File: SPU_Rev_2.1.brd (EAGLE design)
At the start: 141 x 101.6 mm, 236 parts, among them Q1 12MHz, X1 403-5X020-5X

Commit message: renamed to 2.1
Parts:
- added C60, C61, C62, C63, C64, C65, C66, C67: 10u, rcl:E/7260-38W
- added D13: (no value), special:7SEG-13
- added RN_SEG1, RN_SEG2: 220, resistor-dil:0603-ARC
- moved C57 51.4 mm to (14.5, 21.0), turned to 270 degrees
- moved C53 49.4 mm to (29.1, 18.5), flipped to the bottom
- moved C51 49.3 mm to (29.3, 19.3), turned to 90 degrees
- moved C59 49.0 mm to (14.9, 19.4), flipped to the bottom, turned to 90 degrees
- moved C58 48.2 mm to (14.5, 18.4), turned to 180 degrees
- moved X_RXSM-DAPI 47.2 mm to (135.9, 65.8)
- moved C47 46.6 mm to (36.4, 21.8), turned to 90 degrees
- moved C54 46.2 mm to (22.6, 21.7), turned to 90 degrees
- moved R57 46.1 mm to (20.2, 19.1), turned to 180 degrees
- moved C45 46.0 mm to (39.1, 19.2), turned to 270 degrees
- moved C50 46.0 mm to (27.2, 16.3), turned to 90 degrees
- moved C46 45.2 mm to (40.1, 15.9), turned to 270 degrees
- moved R50 44.4 mm to (35.4, 19.3), turned to 180 degrees
- moved R17 43.3 mm to (121.0, 59.9), turned to 270 degrees
- moved R63 42.8 mm to (15.0, 22.9), flipped to the bottom
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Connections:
- new net N$126: D13.7, RN_SEG1.8
- new net N$140: D13.6, RN_SEG1.7
- new net N$142: D13.4, RN_SEG1.6
- new net N$143: D13.2, RN_SEG1.5
- new net N$144: D13.1, RN_SEG2.8
- new net N$145: D13.9, RN_SEG2.7
- new net N$146: D13.10, RN_SEG2.6
- new net N$147: D13.5, RN_SEG2.5
- new net N$149: RN_SEG2.1
- new net N$150: RN_SEG1.4
- new net N$151: RN_SEG1.3
- new net N$152: RN_SEG1.2
- new net N$153: RN_SEG1.1
- new net N$154: RN_SEG2.2
- new net N$155: RN_SEG2.3
- new net N$156: RN_SEG2.4
- net 28V: now also C60.+, C61.+, C62.+
- net 28VGND: now also C60.-, C61.-, C62.-
- net 3V3: now also C67.+, D13.3, D13.8
- net 5V: now also C63.+, C64.+, C65.+, C66.+
- net GND: now also C63.-, C64.-, C65.-, C66.-, C67.-
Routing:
- net DMS63: track 0.00 -> 14.0 mm
- net DMS41: track 0.00 -> 12.9 mm
- net DMS62: track 0.00 -> 12.6 mm
- net DMS42: track 0.00 -> 11.6 mm
- net DMS61: track 0.00 -> 11.5 mm
- net DMS43: track 0.00 -> 10.1 mm
- net DMS51: track 0.00 -> 3.85 mm
- net DMS53: track 0.00 -> 3.64 mm
- net DMS52: track 0.00 -> 3.32 mm

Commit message: foo
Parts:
- removed D13: (no value), special:7SEG-13
- removed RN_SEG1, RN_SEG2: 220, resistor-dil:0603-ARC
- added C68, C69, C70, C71: 10u, rcl:E/7260-38W
- added X_GPIO: 403-5X020-5X, con-ept-One27:403-5X020-5X
- moved X_MIRROR 69.1 mm to (120.5, 83.6)
- moved X_MIRROR1 69.1 mm to (120.5, 83.6)
- moved C2 47.0 mm to (84.3, 86.9), turned to 270 degrees
- moved Q1 45.4 mm to (90.7, 91.9), turned to 180 degrees
- moved D2 40.3 mm to (97.0, 91.9), turned to 0 degrees
- moved U_OPTO_2 35.6 mm to (108.2, 90.8), turned to 0 degrees
- moved U_CH340G 35.5 mm to (90.7, 81.8), turned to 180 degrees
- moved C1 34.2 mm to (97.0, 86.9), turned to 270 degrees
- moved D1 32.8 mm to (97.0, 85.6), turned to 0 degrees
- moved RN12 30.0 mm to (108.1, 87.1), turned to 90 degrees
- moved C42 29.6 mm to (96.7, 56.2), turned to 180 degrees
- moved C33 27.9 mm to (97.0, 81.0), turned to 90 degrees
- moved C62 27.7 mm to (111.6, 69.2), turned to 90 degrees
- moved U_OPTO_1 25.2 mm to (108.2, 83.8), turned to 0 degrees
- moved RN11 23.6 mm to (101.9, 79.4), turned to 0 degrees
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- renumbered X1 to X_DMS
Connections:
- removed net N$126: D13.7, RN_SEG1.8
- removed net N$140: D13.6, RN_SEG1.7
- removed net N$142: D13.4, RN_SEG1.6
- removed net N$143: D13.2, RN_SEG1.5
- removed net N$144: D13.1, RN_SEG2.8
- removed net N$145: D13.9, RN_SEG2.7
- removed net N$146: D13.10, RN_SEG2.6
- removed net N$147: D13.5, RN_SEG2.5
- removed net N$149: RN_SEG2.1
- removed net N$150: RN_SEG1.4
- removed net N$151: RN_SEG1.3
- removed net N$152: RN_SEG1.2
- removed net N$153: RN_SEG1.1
- removed net N$154: RN_SEG2.2
- removed net N$155: RN_SEG2.3
- removed net N$156: RN_SEG2.4
- net 3V3: now also C68.+, C69.+, C70.+, C71.+, X_GPIO.P$B1, X_GPIO.P$B2; no longer D13.3, D13.8
- net GND: now also C68.-, C69.-, C70.-, C71.-, X_GPIO.P$A1, X_GPIO.P$A2
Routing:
- net 28V: track 9.34 -> 97.4 mm, vias 1 -> 8
- net 5V: track 0.00 -> 37.2 mm, vias 0 -> 6
- net GND: track 37.8 -> 51.7 mm, vias 1 -> 186
- net 3V3: track 21.2 -> 32.3 mm, vias 2 -> 8
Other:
- board size 141 x 101.6 mm -> 127.6 x 101.6 mm

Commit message: viafence STRUCT
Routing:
- net GND: vias 186 -> 56
- added copper zone on layer 1, net STRUCT
- added copper zone on layer 15, net STRUCT
- added copper zone on layer 16, net STRUCT
- added copper zone on layer 2, net STRUCT

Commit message: foo
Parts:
- added C72, C73: 10u, rcl:E/7260-38W
- moved D10 35.4 mm to (99.6, 69.1), turned to 270 degrees
- moved D3 27.0 mm to (90.4, 71.6), turned to 0 degrees
- moved D4 25.9 mm to (90.4, 67.9), turned to 0 degrees
- moved RN11 18.1 mm to (114.6, 92.3), flipped to the bottom, turned to 270 degrees
- moved C36 13.5 mm to (96.3, 11.7), turned to 90 degrees
- moved R48 4.70 mm to (47.0, 22.1), turned to 180 degrees
- moved R49 3.68 mm to (42.8, 22.1), turned to 0 degrees
- moved C69 3.41 mm to (84.2, 85.0), turned to 270 degrees
- moved RN_B_PT3 1.45 mm to (18.3, 93.6)
- moved C62 1.13 mm to (111.8, 68.1)
- moved R44 0.97 mm to (45.3, 14.1)
- moved RN_A_PT3 0.97 mm to (14.5, 93.6)
- moved C56 0.89 mm to (13.6, 13.8)
- moved C43 0.85 mm to (97.7, 44.6)
- moved R29 0.52 mm to (56.8, 61.8), turned to 270 degrees
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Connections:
- net 3V3: now also C72.+, C73.+, U_CH340G.4
- net GND: now also C72.-, C73.-
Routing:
- net 3V3: track 32.3 -> 819.0 mm, vias 8 -> 37
- net 5V: track 37.2 -> 192.9 mm, vias 6 -> 7
- net 28V: track 97.4 -> 220.3 mm, vias 8 -> 11
- net 5V-28V: track 0.00 -> 73.8 mm, vias 0 -> 1
- net EXP_IN_OPT: track 0.00 -> 57.6 mm, vias 0 -> 1
- net GND: track 51.7 -> 94.6 mm, vias 56 -> 64
- net EXP_OUT_OPT: track 0.00 -> 36.4 mm
- net DAPI_RX: track 0.00 -> 35.7 mm, vias 0 -> 2
- net DAPI_TX: track 0.00 -> 19.9 mm, vias 0 -> 2
- net N$3: track 0.00 -> 18.4 mm
- net LO: track 2.12 -> 20.5 mm, vias 1 -> 2
- net EXP_IN: track 0.00 -> 16.7 mm, vias 0 -> 2
- net SODS: track 2.12 -> 15.7 mm
- net N$42: track 0.00 -> 13.1 mm, vias 0 -> 1
- net SOE: track 2.12 -> 14.7 mm
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- added copper zone on layer 1, net 28VGND
- added copper zone on layer 15, net 28VGND
- added copper zone on layer 16, net 28VGND
- added copper zone on layer 2, net 28VGND

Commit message: some routing
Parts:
- moved C68 0.65 mm to (50.2, 83.7)
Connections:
- removed net ADC1_DRDY: U_STM32F779.65
- removed net ADC1_RES: U_STM32F779.68
- removed net ADC1_START: U_STM32F779.67
- removed net ADC2_DRDY: U_STM32F779.47
- removed net ADC2_RES: U_STM32F779.50
- removed net ADC2_START: U_STM32F779.49
- removed net ADC3_DRDY: U_STM32F779.71
- removed net ADC3_RES: U_STM32F779.76
- removed net ADC3_START: U_STM32F779.75
- removed net ADC4_DRDY: U_STM32F779.32
- removed net ADC4_RES: U_STM32F779.31
- removed net ADC4_START: U_STM32F779.30
- removed net ADC5_DRDY: U_STM32F779.44
- removed net ADC5_RES: U_STM32F779.37
- removed net ADC5_START: U_STM32F779.35
- removed net ADC6_DRDY: U_STM32F779.45
- removed net ADC6_RES: U_STM32F779.33
- removed net ADC6_START: U_STM32F779.38
- removed net OUT_PT_1: U_STM32F779.62
- removed net OUT_PT_2: U_STM32F779.53
- removed net OUT_PT_3: U_STM32F779.61
- removed net SPI3_CS: U_STM32F779.66
- removed net SPI3_CS2: U_STM32F779.18
- removed net SPI3_MISO: U_STM32F779.162
- removed net SPI3_MOSI: U_STM32F779.63
- removed net SPI3_SCK: U_STM32F779.161
- removed net SPI4_CS: U_STM32F779.48
- removed net SPI4_CS2: U_STM32F779.19
- removed net SPI4_MISO: U_STM32F779.4
- removed net SPI4_MOSI: U_STM32F779.5
- removed net SPI4_SCK: U_STM32F779.1
- removed net SPI5_CS: U_STM32F779.74
- removed net SPI5_CS2: U_STM32F779.20
- removed net SPI5_MISO: U_STM32F779.29
- removed net SPI5_MOSI: U_STM32F779.70
- removed net SPI5_SCK: U_STM32F779.28
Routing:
- net DAPI_P: track 9.31 -> 56.8 mm, vias 1 -> 2
- net DAPI_N: track 8.37 -> 53.7 mm, vias 1 -> 2
- net PT22: track 0.00 -> 40.3 mm
- net GND: track 94.6 -> 133.2 mm
- net FL_1_WP: track 0.00 -> 37.8 mm
- net TMS: track 0.00 -> 37.7 mm, vias 0 -> 1
- net EXP_OUT_N: track 0.00 -> 36.0 mm, vias 0 -> 2
- net TRST: track 0.00 -> 35.6 mm, vias 0 -> 1
- net FL_1_CS1: track 0.00 -> 33.5 mm, vias 0 -> 2
- net EXP_OUT_P: track 0.00 -> 31.7 mm, vias 0 -> 2
- net NRST: track 0.00 -> 28.9 mm, vias 0 -> 1
- net FL_2_WP: track 0.00 -> 28.8 mm, vias 0 -> 2
- net EXP_IN_N: track 2.16 -> 30.4 mm, vias 0 -> 2
- net FL_2_CS1: track 0.00 -> 27.9 mm, vias 0 -> 2
- net PT21: track 0.00 -> 26.5 mm
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
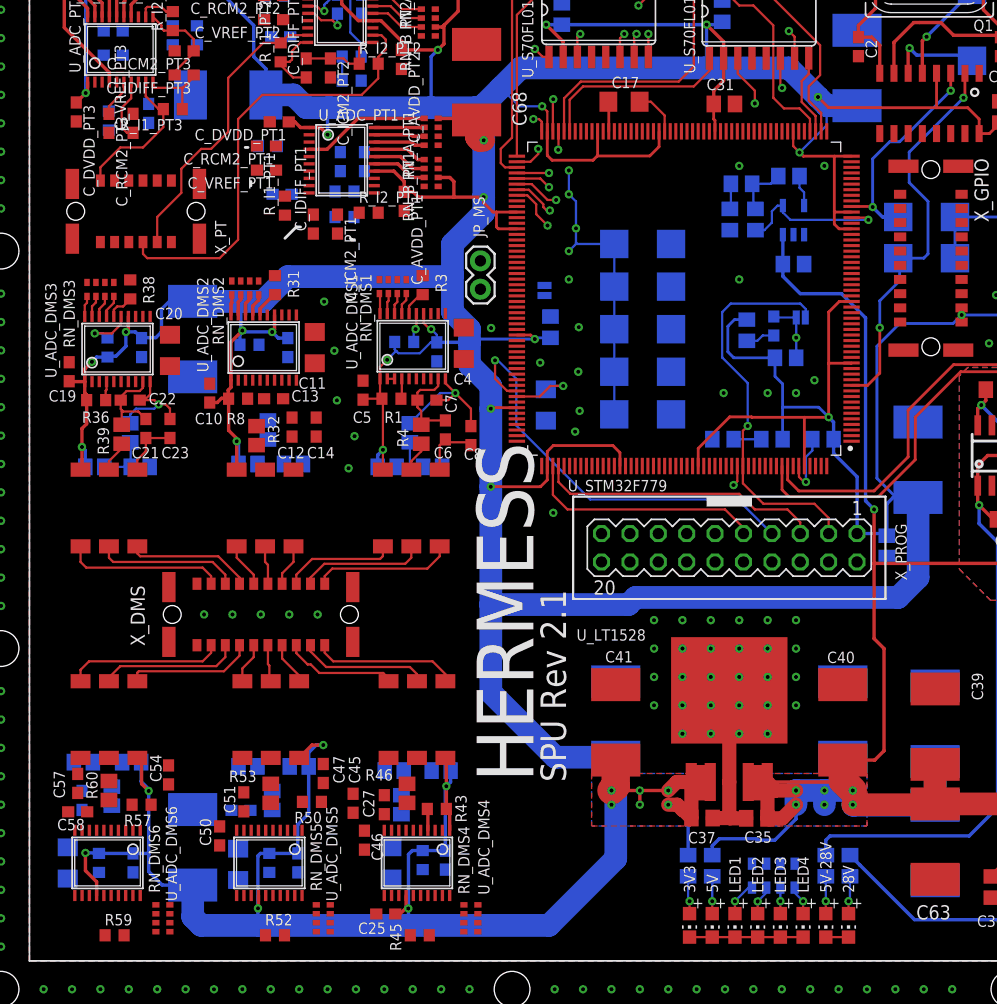
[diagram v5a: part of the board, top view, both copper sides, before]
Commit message: Pins matched to Cube
next step, autoroute (if possible)
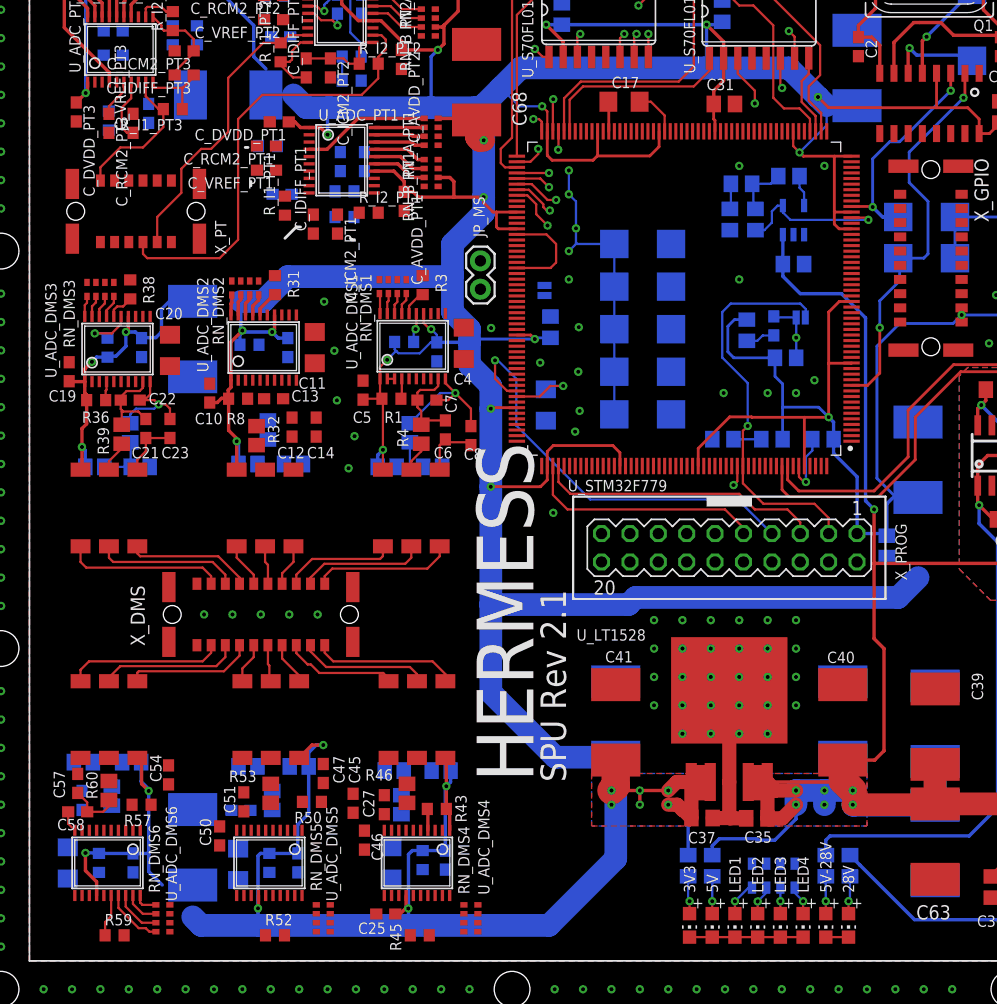
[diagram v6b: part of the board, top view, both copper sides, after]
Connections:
- removed net DMS_DIN: RN_DMS1.7, RN_DMS2.7, RN_DMS3.7, RN_DMS4.7, RN_DMS5.7, RN_DMS6.7
- removed net DMS_DOUT: RN_DMS1.6, RN_DMS2.6, RN_DMS3.6, RN_DMS4.6, RN_DMS5.6, RN_DMS6.6
- removed net DMS_SCLK: RN_DMS1.8, RN_DMS2.8, RN_DMS3.8, RN_DMS4.8, RN_DMS5.8, RN_DMS6.8
- removed net N$148: X_DMS.P$B10
- removed net N$157: X_DMS.P$A10
- removed net N$17: X_PT.P$A6
- removed net N$18: X_PT.P$A5
- removed net N$19: X_PT.P$A4
- removed net PT_DIN: RN_A_PT1.6, RN_A_PT2.6, RN_A_PT3.6
- removed net PT_DOUT: RN_A_PT1.5, RN_A_PT2.5, RN_A_PT3.5
- removed net PT_SCLK: RN_A_PT1.7, RN_A_PT2.7, RN_A_PT3.7
- new net SPI3_MISO: RN_A_PT1.5, RN_A_PT2.5, RN_A_PT3.5, U_STM32F779.162
- new net SPI3_MOSI: RN_A_PT1.6, RN_A_PT2.6, RN_A_PT3.6, U_STM32F779.63
- new net SPI3_SCK: RN_A_PT1.7, RN_A_PT2.7, RN_A_PT3.7, U_STM32F779.161
- new net SPI4_MISO: RN_DMS1.6, RN_DMS2.6, RN_DMS3.6, RN_DMS4.6, RN_DMS5.6, RN_DMS6.6, U_STM32F779.4
- new net SPI4_MOSI: RN_DMS1.7, RN_DMS2.7, RN_DMS3.7, RN_DMS4.7, RN_DMS5.7, RN_DMS6.7, U_STM32F779.5
- new net SPI4_SCK: RN_DMS1.8, RN_DMS2.8, RN_DMS3.8, RN_DMS4.8, RN_DMS5.8, RN_DMS6.8, U_STM32F779.1
- net !CS!_DMS1: now also U_STM32F779.74
- net !CS!_DMS2: now also U_STM32F779.75
- net !CS!_DMS3: now also U_STM32F779.76
- net !CS!_DMS4: now also U_STM32F779.77
- net !CS!_DMS5: now also U_STM32F779.78
- net !CS!_DMS6: now also U_STM32F779.79
- net !CS!_PT1: now also U_STM32F779.117
- net !CS!_PT2: now also U_STM32F779.116
- net !CS!_PT3: now also U_STM32F779.108
- net !DRDY!_DMS1: now also U_STM32F779.131
- net !DRDY!_DMS2: now also U_STM32F779.142
- net !DRDY!_DMS3: now also U_STM32F779.143
- net !DRDY!_DMS4: now also U_STM32F779.144
- net !DRDY!_DMS5: now also U_STM32F779.145
- net !DRDY!_DMS6: now also U_STM32F779.146
- net !DRDY!_PT1: now also U_STM32F779.177
- net !DRDY!_PT2: now also U_STM32F779.176
- net !DRDY!_PT3: now also U_STM32F779.175
- net FL_2_WP: now also U_STM32F779.113; no longer U_STM32F779.108
- net GND: now also X_DMS.P$A10, X_DMS.P$B10, X_PT.P$A4, X_PT.P$A5, X_PT.P$A6
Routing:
- net 3V3: track 821.4 -> 792.6 mm
- net N$36: track 0.00 -> 9.23 mm
- net N$138: track 0.00 -> 5.34 mm
- net N$128: track 0.00 -> 4.74 mm
- net N$137: track 0.00 -> 4.29 mm
- net N$139: track 0.00 -> 3.78 mm
- net N$136: track 0.00 -> 3.17 mm
- net N$135: track 0.00 -> 2.13 mm
- net N$129: track 0.00 -> 1.90 mm

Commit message: cleanup autoroute 1/inf
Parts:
- moved RN_B_PT2 1.17 mm to (44.7, 88.8)
- moved RN_B_PT3 1.15 mm to (18.4, 92.5)
- moved RN_B_PT1 0.63 mm to (45.5, 75.6)
- moved C_AVDD_PT2 0.62 mm to (43.2, 85.1)
- moved C68 0.52 mm to (50.3, 84.2)
- moved C_DVDD_PT2 0.23 mm to (32.8, 93.8)
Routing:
- net GND: track 133.2 -> 1186.4 mm, vias 64 -> 102
- net SPI4_SCK: track 0.00 -> 231.9 mm, vias 0 -> 7
- net SPI4_MISO: track 0.00 -> 216.5 mm, vias 0 -> 8
- net SPI4_MOSI: track 0.00 -> 200.0 mm, vias 0 -> 7
- net !CS!_DMS6: track 0.00 -> 115.6 mm, vias 0 -> 4
- net INTERSPU_TX: track 3.86 -> 111.8 mm, vias 1 -> 5
- net SODS_OPT: track 0.00 -> 105.6 mm, vias 0 -> 4
- net !CS!_DMS5: track 0.00 -> 103.2 mm, vias 0 -> 3
- net LED_4: track 0.00 -> 98.8 mm, vias 0 -> 3
- net SPI3_MOSI: track 0.00 -> 98.4 mm, vias 0 -> 5
- net LO_OPT: track 0.00 -> 93.5 mm, vias 0 -> 4
- net !CS!_DMS4: track 0.00 -> 92.4 mm
- net !DRDY!_DMS6: track 0.00 -> 91.1 mm, vias 0 -> 2
- net SOE_OPT: track 0.00 -> 84.9 mm, vias 0 -> 4
- net !DRDY!_PT3: track 0.00 -> 80.1 mm, vias 0 -> 2
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
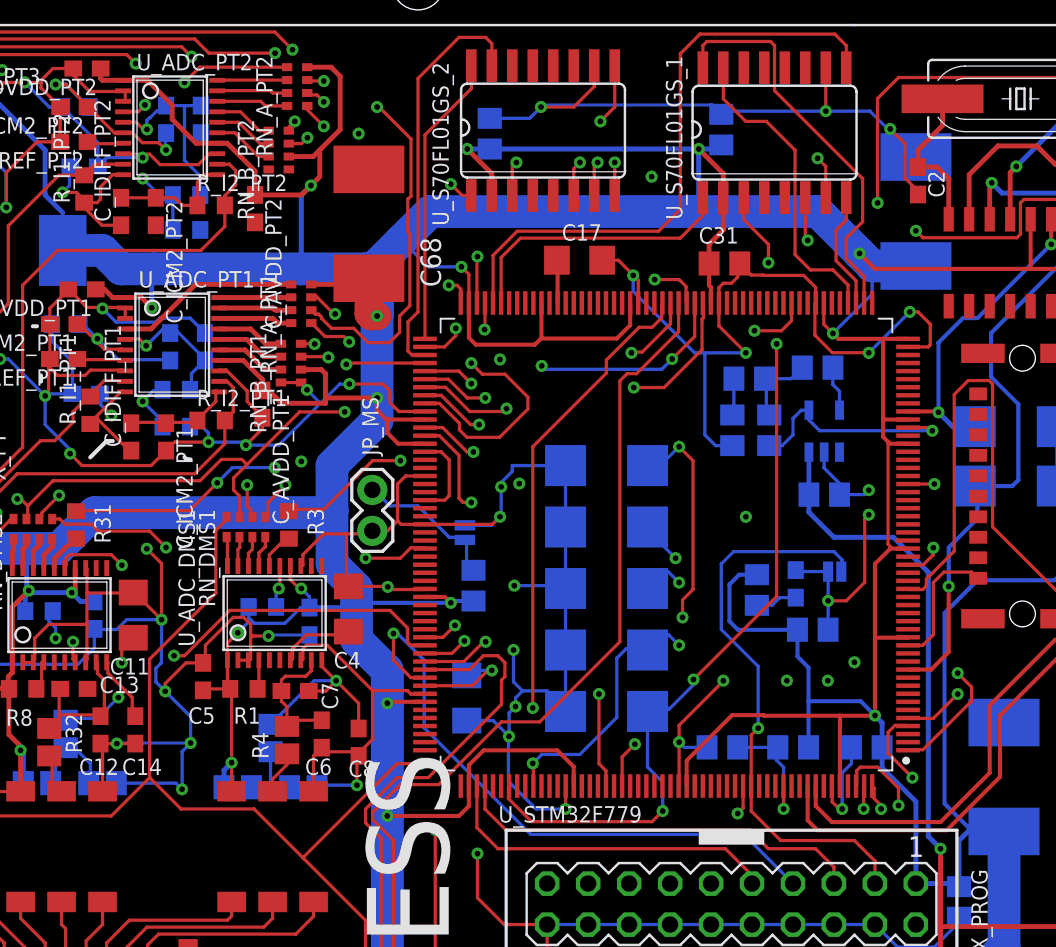
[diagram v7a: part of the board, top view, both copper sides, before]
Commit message: fix autoroute 2/inf
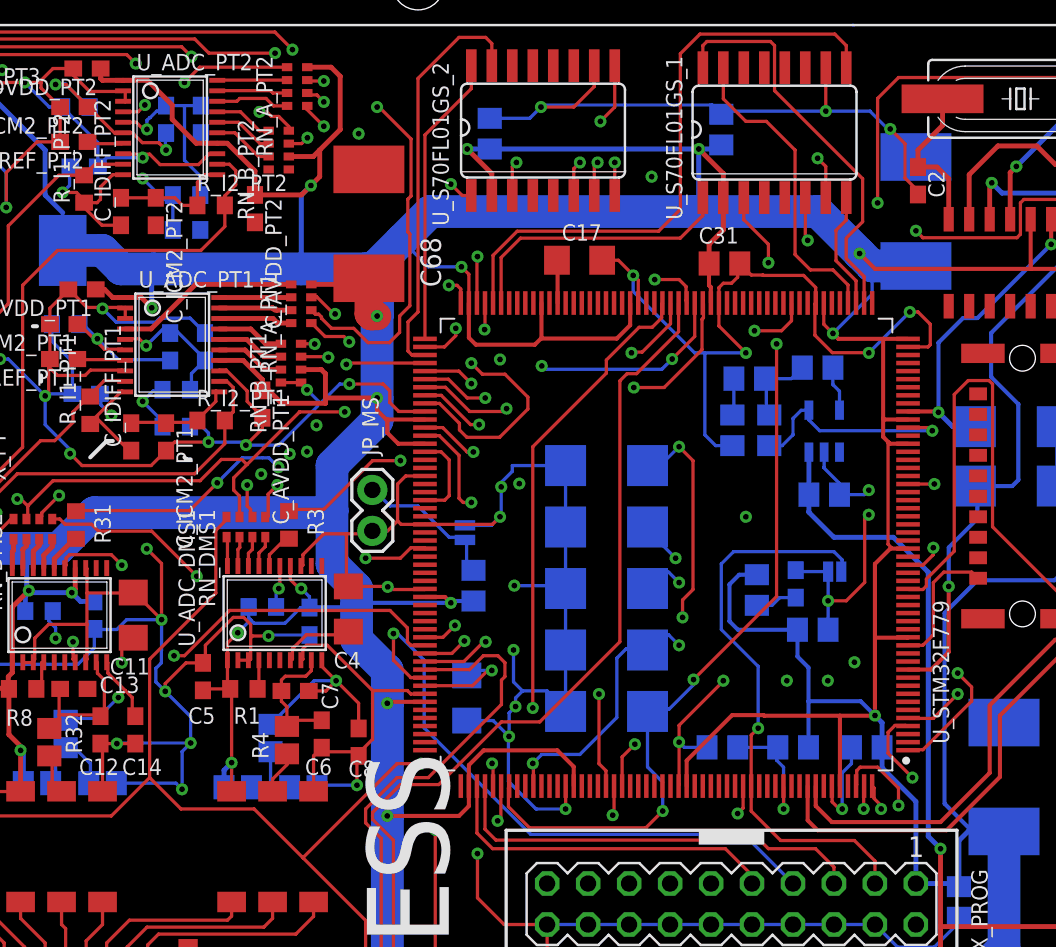
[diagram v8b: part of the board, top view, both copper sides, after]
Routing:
- net SPI3_MISO: track 52.8 -> 106.8 mm, vias 3 -> 5
- net SPI3_SCK: track 53.5 -> 102.5 mm, vias 3 -> 6
- net !DRDY!_PT2: track 0.73 -> 4.29 mm, vias 1 -> 2
- net !DRDY!_PT3: track 80.1 -> 81.4 mm
- net !CS!_DMS2: track 48.5 -> 49.3 mm
- net TDI: track 25.6 -> 26.3 mm
- net INTERSPU_TX: track 111.8 -> 112.4 mm
